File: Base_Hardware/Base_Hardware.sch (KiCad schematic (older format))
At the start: 23 parts

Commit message: Created Base Schematic
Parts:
- removed J?: NEO Out, symbol Connector:Conn_01x03_Male
- added J?: NEO Out, symbol Connector:Conn_01x03_Female
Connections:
- net +5V: now also J?.1 (Pin_1)
- net DOut': now also J?.2 (Pin_2)
- net GND: now also J?.3 (Pin_3)
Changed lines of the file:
@@
 DOut'
-$Comp
-L Connector:Conn_01x03_Male J?
-U 1 1 5EDAC209
-P 4100 1850
-F 0 "J?" H 4206 2128 50  0000 C CNN
-F 1 "NEO Out" H 4206 2037 50  0000 C CNN
-F 2 "" H 4100 1850 50  0001 C CNN
-F 3 "~" H 4100 1850 50  0001 C CNN
-	1    4100 1850
-	1    0    0    -1
-$EndComp
 $Comp
 L power:+5V #PWR?
 U 1 1 5EDAC2CF
-P 4400 1650
-F 0 "#PWR?" H 4400 1500 50  0001 C CNN
-F 1 "+5V" H 4415 1823 50  0000 C CNN
-F 2 "" H 4400 1650 50  0001 C CNN
-F 3 "" H 4400 1650 50  0001 C CNN
-	1    4400 1650
-	1    0    0    -1
+P 4300 1650
+F 0 "#PWR?" H 4300 1500 50  0001 C CNN
+F 1 "+5V" H 4315 1823 50  0000 C CNN
+F 2 "" H 4300 1650 50  0001 C CNN
+F 3 "" H 4300 1650 50  0001 C CNN
+	1    4300 1650
+	-1   0    0    -1
 $EndComp
 $Comp
 L power:GND #PWR?
 U 1 1 5EDAC32A
-P 4400 2050
-F 0 "#PWR?" H 4400 1800 50  0001 C CNN
-F 1 "GND" H 4405 1877 50  0000 C CNN
-F 2 "" H 4400 2050 50  0001 C CNN
-F 3 "" H 4400 2050 50  0001 C CNN
-	1    4400 2050
-	1    0    0    -1
-$EndComp
-Wire Wire Line
-	4300 1750 4400 1750
-Wire Wire Line
-	4400 1750 4400 1650
-Wire Wire Line
-	4300 1950 4400 1950
-Wire Wire Line
-	4400 1950 4400 2050
-Text GLabel 4400 1850 2    50   Input ~ 0
+P 4300 2050
+F 0 "#PWR?" H 4300 1800 50  0001 C CNN
+F 1 "GND" H 4305 1877 50  0000 C CNN
+F 2 "" H 4300 2050 50  0001 C CNN
+F 3 "" H 4300 2050 50  0001 C CNN
+	1    4300 2050
+	-1   0    0    -1
+$EndComp
+Wire Wire Line
+	4400 1750 4300 1750
+Wire Wire Line
+	4300 1750 4300 1650
+Wire Wire Line
+	4400 1950 4300 1950
+Wire Wire Line
+	4300 1950 4300 2050
+Text GLabel 4300 1850 0    50   Input ~ 0
 DOut'
 Wire Wire Line
-	4300 1850 4400 1850
+	4400 1850 4300 1850
 Wire Notes Line
 	2750 1250 2750 2550
@@
 Text Notes 4900 2850 0    197  ~ 39
 Int
+$Comp
+L Connector:Conn_01x03_Female J?
+U 1 1 5EE06865
+P 4600 1850
+F 0 "J?" H 4500 1700 50  0000 L CNN
+F 1 "NEO Out" H 4350 2100 50  0000 L CNN
+F 2 "" H 4600 1850 50  0001 C CNN
+F 3 "~" H 4600 1850 50  0001 C CNN
+	1    4600 1850
+	1    0    0    -1
+$EndComp
 $EndSCHEMATC

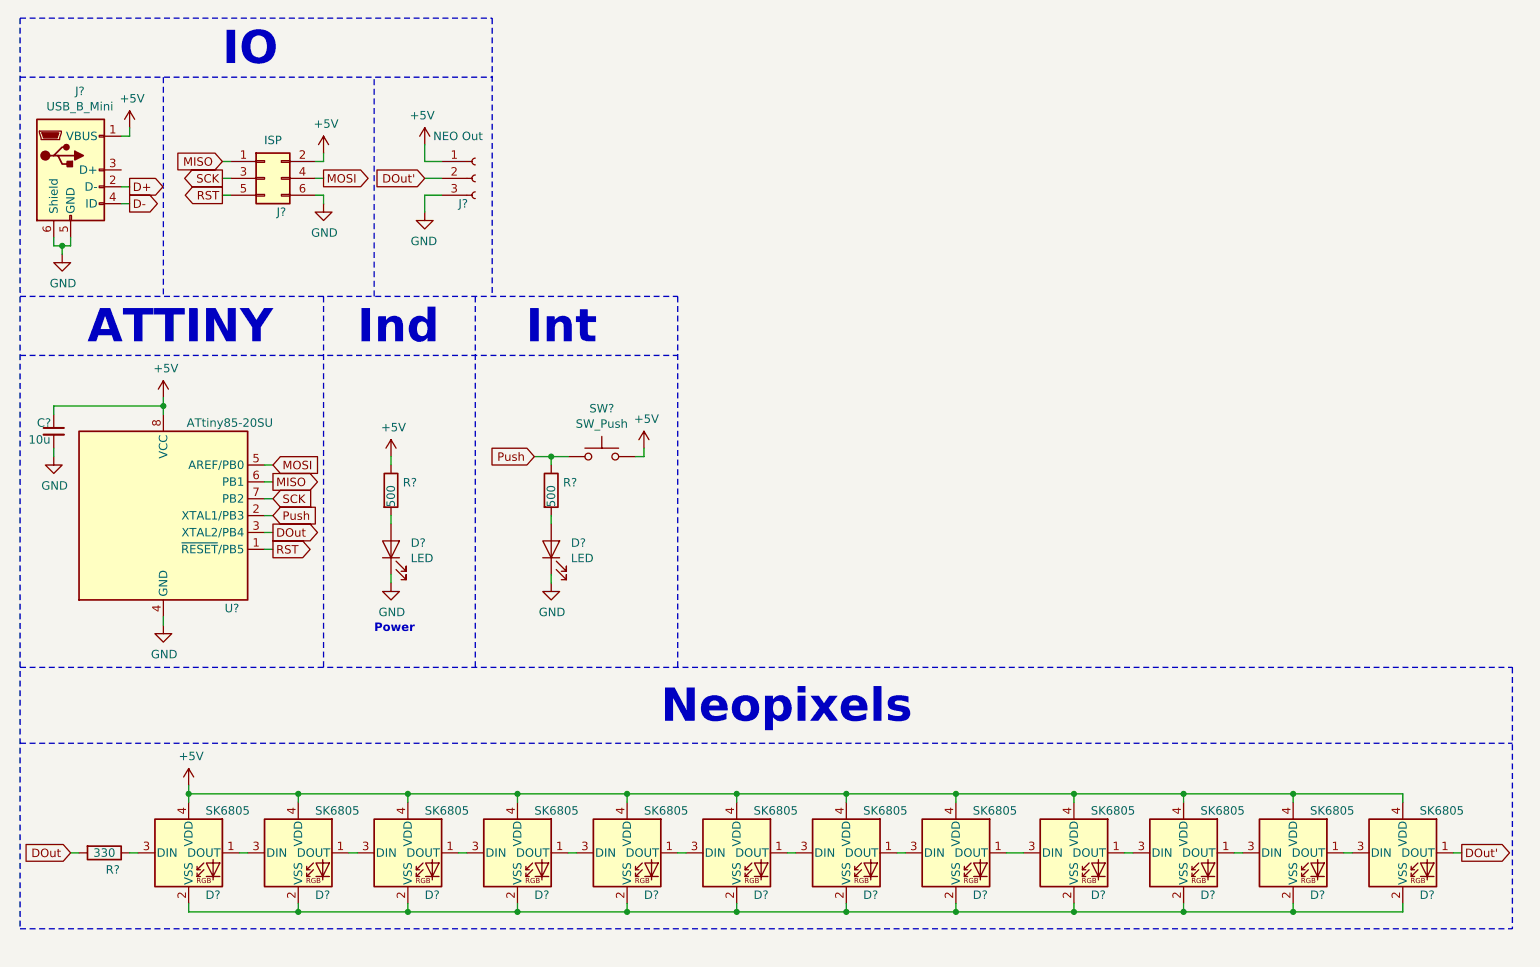
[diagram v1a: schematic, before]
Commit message: assigned footprints
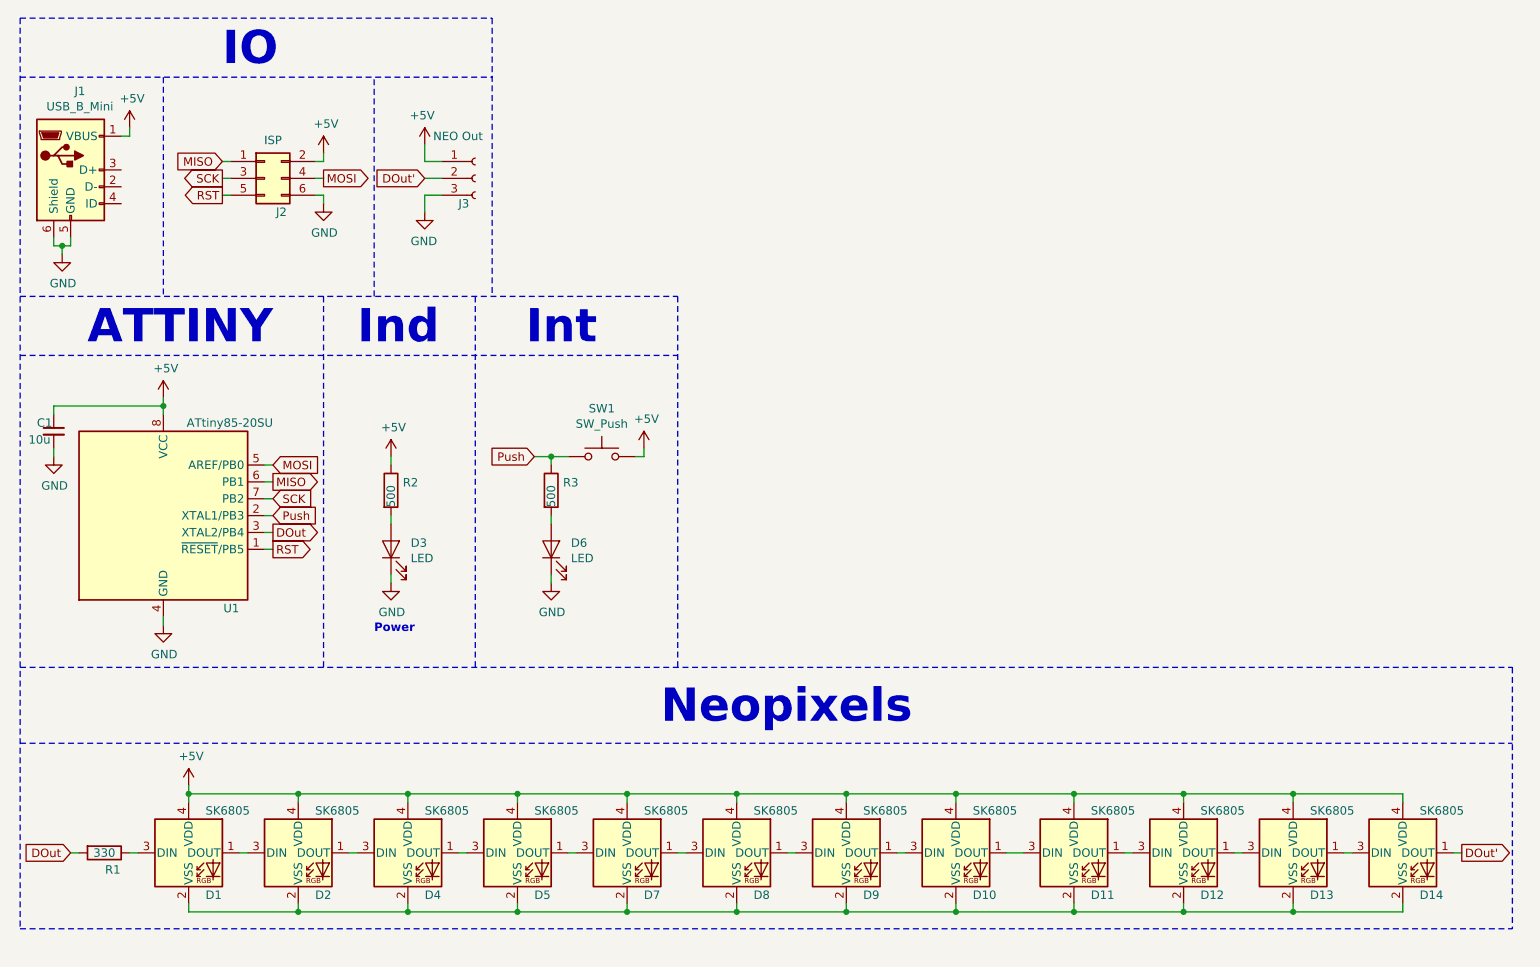
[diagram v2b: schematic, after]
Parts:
- C1: renamed from C?; footprint (none) -> Capacitor_SMD:C_0603_1608Metric_Pad1.05x0.95mm_HandSolder
- D3, D6: renamed from D?; footprint (none) -> LED_SMD:LED_0603_1608Metric_Pad1.05x0.95mm_HandSolder
- J1: renamed from J?; footprint (none) -> ProjectLibrary:MiniUSB_SMD
- J2: renamed from J?; footprint (none) -> Connector_IDC:IDC-Header_2x03_P2.54mm_Vertical
- J3: renamed from J?; footprint (none) -> Connector_PinSocket_2.54mm:PinSocket_1x03_P2.54mm_Horizontal
- R1, R2, R3: renamed from R?; footprint (none) -> Resistor_SMD:R_0603_1608Metric_Pad1.05x0.95mm_HandSolder
- SW1: renamed from SW?; footprint (none) -> Button_Switch_SMD:SW_SPST_PTS645
- gave numbers to parts that had none: 13
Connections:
- net D+: no longer names the net of J1.2 (D-)
- net D-: no longer names the net of J1.4 (ID)

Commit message: modified connecting slit
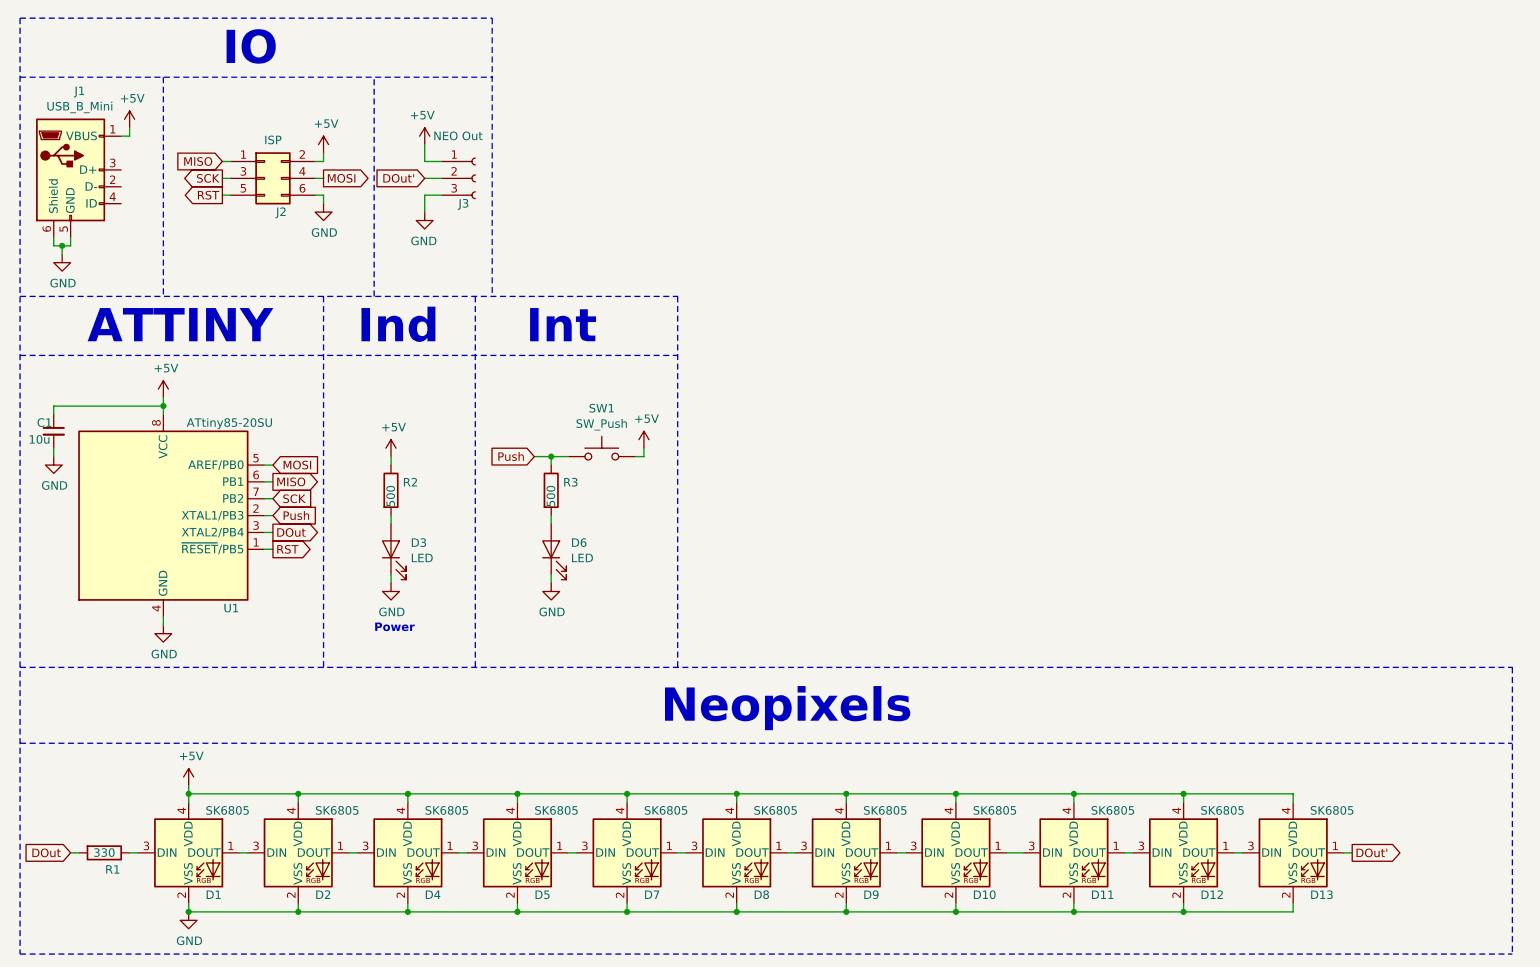
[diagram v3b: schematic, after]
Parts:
- removed D14: SK6805, LED_SMD:LED_SK6805_PLCC4_2.4x2.7mm_P1.3mm, symbol LED:SK6805
- D1, D10, D11, D12, D13, D2, D4, D5, D7, D8, D9: footprint LED_SMD:LED_SK6805_PLCC4_2.4x2.7mm_P1.3mm -> ProjectLibrary:SK6805-EC
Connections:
- net DOut': now also D13.1 (DOUT)
- net GND: now also D1.2 (VSS), D10.2 (VSS), D11.2 (VSS), D12.2 (VSS), D13.2 (VSS), D2.2 (VSS), D4.2 (VSS), D5.2 (VSS), D7.2 (VSS), D8.2 (VSS), D9.2 (VSS)
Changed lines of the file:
@@
 F 0 "D1" H 3000 5600 50  0000 L CNN
 F 1 "SK6805" H 3000 6100 50  0000 L CNN
-F 2 "LED_SMD:LED_SK6805_PLCC4_2.4x2.7mm_P1.3mm" H 2950 5550 50  0001 L TNN
+F 2 "ProjectLibrary:SK6805-EC" H 2950 5550 50  0001 L TNN
 F 3 "https://cdn-shop.adafruit.com/product-files/3484/3484_Datasheet.pdf" H 3000 5475 50  0001 L TNN
 	1    2900 5850
@@
 F 0 "D2" H 3650 5600 50  0000 L CNN
 F 1 "SK6805" H 3650 6100 50  0000 L CNN
-F 2 "LED_SMD:LED_SK6805_PLCC4_2.4x2.7mm_P1.3mm" H 3600 5550 50  0001 L TNN
+F 2 "ProjectLibrary:SK6805-EC" H 3600 5550 50  0001 L TNN
 F 3 "https://cdn-shop.adafruit.com/product-files/3484/3484_Datasheet.pdf" H 3650 5475 50  0001 L TNN
 	1    3550 5850
@@
 F 0 "D4" H 4300 5600 50  0000 L CNN
 F 1 "SK6805" H 4300 6100 50  0000 L CNN
-F 2 "LED_SMD:LED_SK6805_PLCC4_2.4x2.7mm_P1.3mm" H 4250 5550 50  0001 L TNN
+F 2 "ProjectLibrary:SK6805-EC" H 4250 5550 50  0001 L TNN
 F 3 "https://cdn-shop.adafruit.com/product-files/3484/3484_Datasheet.pdf" H 4300 5475 50  0001 L TNN
 	1    4200 5850
@@
 F 0 "D5" H 4950 5600 50  0000 L CNN
 F 1 "SK6805" H 4950 6100 50  0000 L CNN
-F 2 "LED_SMD:LED_SK6805_PLCC4_2.4x2.7mm_P1.3mm" H 4900 5550 50  0001 L TNN
+F 2 "ProjectLibrary:SK6805-EC" H 4900 5550 50  0001 L TNN
 F 3 "https://cdn-shop.adafruit.com/product-files/3484/3484_Datasheet.pdf" H 4950 5475 50  0001 L TNN
 	1    4850 5850
@@
 F 0 "D7" H 5600 5600 50  0000 L CNN
 F 1 "SK6805" H 5600 6100 50  0000 L CNN
-F 2 "LED_SMD:LED_SK6805_PLCC4_2.4x2.7mm_P1.3mm" H 5550 5550 50  0001 L TNN
+F 2 "ProjectLibrary:SK6805-EC" H 5550 5550 50  0001 L TNN
 F 3 "https://cdn-shop.adafruit.com/product-files/3484/3484_Datasheet.pdf" H 5600 5475 50  0001 L TNN
 	1    5500 5850
@@
 Wire Wire Line
 	5500 5500 5500 5550
-$Comp
-L LED:SK6805 D8
-U 1 1 5ED74A00
-P 6150 5850
-F 0 "D8" H 6250 5600 50  0000 L CNN
-F 1 "SK6805" H 6250 6100 50  0000 L CNN
-F 2 "LED_SMD:LED_SK6805_PLCC4_2.4x2.7mm_P1.3mm" H 6200 5550 50  0001 L TNN
-F 3 "https://cdn-shop.adafruit.com/product-files/3484/3484_Datasheet.pdf" H 6250 5475 50  0001 L TNN
-	1    6150 5850
-	1    0    0    -1
-$EndComp
 Wire Wire Line
 	6150 6150 6150 6200
@@
 F 0 "D9" H 6900 5600 50  0000 L CNN
 F 1 "SK6805" H 6900 6100 50  0000 L CNN
-F 2 "LED_SMD:LED_SK6805_PLCC4_2.4x2.7mm_P1.3mm" H 6850 5550 50  0001 L TNN
+F 2 "ProjectLibrary:SK6805-EC" H 6850 5550 50  0001 L TNN
 F 3 "https://cdn-shop.adafruit.com/product-files/3484/3484_Datasheet.pdf" H 6900 5475 50  0001 L TNN
 	1    6800 5850
@@
 F 0 "D10" H 7550 5600 50  0000 L CNN
 F 1 "SK6805" H 7550 6100 50  0000 L CNN
-F 2 "LED_SMD:LED_SK6805_PLCC4_2.4x2.7mm_P1.3mm" H 7500 5550 50  0001 L TNN
+F 2 "ProjectLibrary:SK6805-EC" H 7500 5550 50  0001 L TNN
 F 3 "https://cdn-shop.adafruit.com/product-files/3484/3484_Datasheet.pdf" H 7550 5475 50  0001 L TNN
 	1    7450 5850
@@
 F 0 "D11" H 8250 5600 50  0000 L CNN
 F 1 "SK6805" H 8250 6100 50  0000 L CNN
-F 2 "LED_SMD:LED_SK6805_PLCC4_2.4x2.7mm_P1.3mm" H 8200 5550 50  0001 L TNN
+F 2 "ProjectLibrary:SK6805-EC" H 8200 5550 50  0001 L TNN
 F 3 "https://cdn-shop.adafruit.com/product-files/3484/3484_Datasheet.pdf" H 8250 5475 50  0001 L TNN
 	1    8150 5850
@@
 F 0 "D12" H 8900 5600 50  0000 L CNN
 F 1 "SK6805" H 8900 6100 50  0000 L CNN
-F 2 "LED_SMD:LED_SK6805_PLCC4_2.4x2.7mm_P1.3mm" H 8850 5550 50  0001 L TNN
+F 2 "ProjectLibrary:SK6805-EC" H 8850 5550 50  0001 L TNN
 F 3 "https://cdn-shop.adafruit.com/product-files/3484/3484_Datasheet.pdf" H 8900 5475 50  0001 L TNN
 	1    8800 5850
@@
 F 0 "D13" H 9550 5600 50  0000 L CNN
 F 1 "SK6805" H 9550 6100 50  0000 L CNN
-F 2 "LED_SMD:LED_SK6805_PLCC4_2.4x2.7mm_P1.3mm" H 9500 5550 50  0001 L TNN
+F 2 "ProjectLibrary:SK6805-EC" H 9500 5550 50  0001 L TNN
 F 3 "https://cdn-shop.adafruit.com/product-files/3484/3484_Datasheet.pdf" H 9550 5475 50  0001 L TNN
 	1    9450 5850
@@
 Wire Wire Line
 	9450 6150 9450 6200
-$Comp
-L LED:SK6805 D14
-U 1 1 5ED8B620
-P 10100 5850
-F 0 "D14" H 10200 5600 50  0000 L CNN
-F 1 "SK6805" H 10200 6100 50  0000 L CNN
-F 2 "LED_SMD:LED_SK6805_PLCC4_2.4x2.7mm_P1.3mm" H 10150 5550 50  0001 L TNN
-F 3 "https://cdn-shop.adafruit.com/product-files/3484/3484_Datasheet.pdf" H 10200 5475 50  0001 L TNN
-	1    10100 5850
-	1    0    0    -1
-$EndComp
-Wire Wire Line
-	10100 6150 10100 6200
-Wire Wire Line
-	10400 5850 10450 5850
+Wire Wire Line
+	9750 5850 9800 5850
 Wire Wire Line
 	2900 5450 2900 5500
@@
 Wire Wire Line
 	8150 5500 8800 5500
-Wire Wire Line
-	10100 5500 10100 5550
 Connection ~ 8150 5500
 Wire Wire Line
 	9450 5550 9450 5500
-Connection ~ 9450 5500
-Wire Wire Line
-	9450 5500 10100 5500
 Wire Wire Line
 	8800 5550 8800 5500
@@
 Wire Wire Line
 	8800 6200 9450 6200
-Connection ~ 9450 6200
-Wire Wire Line
-	9450 6200 10100 6200
-Wire Wire Line
-	9800 5850 9750 5850
 Wire Wire Line
 	9150 5850 9100 5850
@@
 Wire Wire Line
 	3250 5850 3200 5850
-Text GLabel 10450 5850 2    50   Output ~ 0
+Text GLabel 9800 5850 2    50   Output ~ 0
 DOut'
 $Comp
@@
 Wire Notes Line
 	1900 5200 10750 5200
-Wire Notes Line
-	1900 6300 10750 6300
 Text Notes 5700 5100 0    197  ~ 39
 Neopixels
 Wire Notes Line
-	10750 4750 10750 6300
-Wire Notes Line
 	1900 4750 10750 4750
-Wire Notes Line
-	1900 900  1900 6300
 $Comp
 L Device:LED D3
@@
 	1    0    0    -1
 $EndComp
+$Comp
+L power:GND #PWR0115
+U 1 1 5EDBDD3F
+P 2900 6200
+F 0 "#PWR0115" H 2900 5950 50  0001 C CNN
+F 1 "GND" H 2905 6027 50  0000 C CNN
+F 2 "" H 2900 6200 50  0001 C CNN
+F 3 "" H 2900 6200 50  0001 C CNN
+	1    2900 6200
+	1    0    0    -1
+$EndComp
+Connection ~ 2900 6200
+Wire Notes Line
+	1900 6450 10750 6450
+Wire Notes Line
+	10750 4750 10750 6450
+Wire Notes Line
+	1900 900  1900 6450
+$Comp
+L LED:SK6805 D8
+U 1 1 5EDC36C0
+P 6150 5850
+F 0 "D8" H 6250 5600 50  0000 L CNN
+F 1 "SK6805" H 6250 6100 50  0000 L CNN
+F 2 "ProjectLibrary:SK6805-EC" H 6200 5550 50  0001 L TNN
+F 3 "https://cdn-shop.adafruit.com/product-files/3484/3484_Datasheet.pdf" H 6250 5475 50  0001 L TNN
+	1    6150 5850
+	1    0    0    -1
+$EndComp

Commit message: Placed high-level components and traces
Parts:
- J3: footprint Connector_PinSocket_2.54mm:PinSocket_1x03_P2.54mm_Horizontal -> Connector_PinSocket_2.54mm:PinSocket_1x03_P2.54mm_Vertical
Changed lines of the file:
@@
 F 0 "J3" H 4500 1700 50  0000 L CNN
 F 1 "NEO Out" H 4350 2100 50  0000 L CNN
-F 2 "Connector_PinSocket_2.54mm:PinSocket_1x03_P2.54mm_Horizontal" H 4600 1850 50  0001 C CNN
+F 2 "Connector_PinSocket_2.54mm:PinSocket_1x03_P2.54mm_Vertical" H 4600 1850 50  0001 C CNN
 F 3 "~" H 4600 1850 50  0001 C CNN
 	1    4600 1850
